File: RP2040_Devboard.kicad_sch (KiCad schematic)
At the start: 39 parts, among them J1 USB_B_Mini, J2 Conn_01x03_Socket, J3 Conn_01x22, J5 Conn_01x22, SW1 SW_Push, SW2 SW_Push, U1 RP2040, U2 AP2112K-1.2, U3 USBLC6-2SC6, U4 W25Q128JVS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

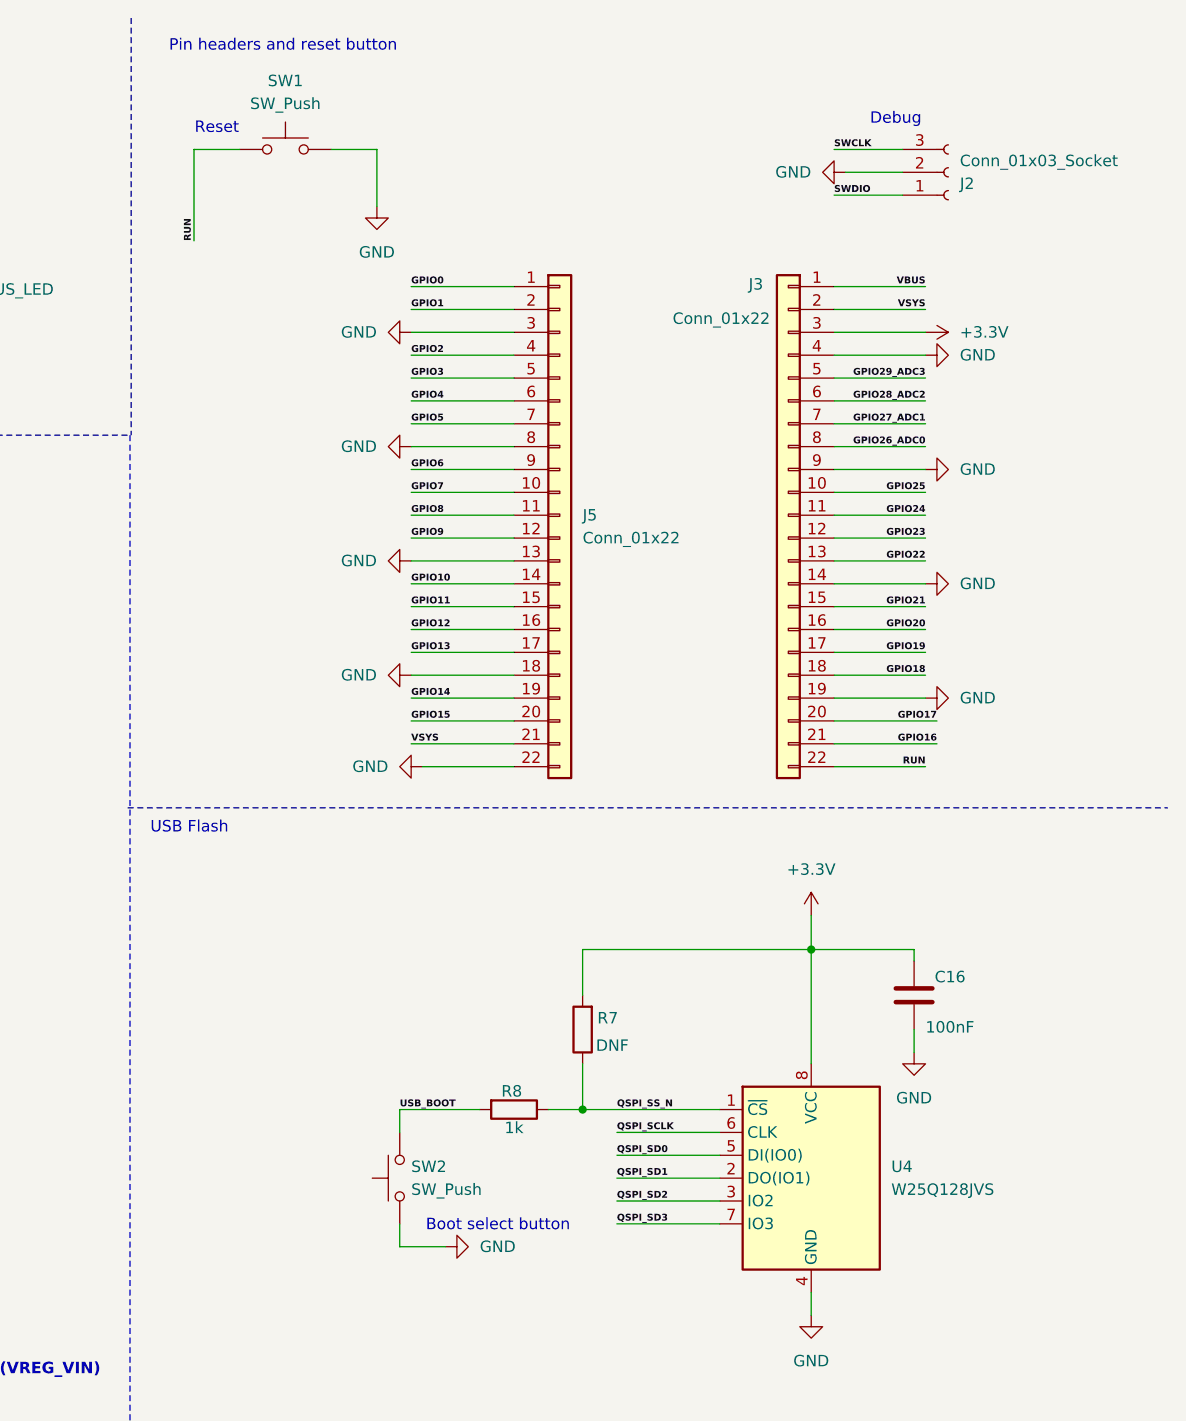
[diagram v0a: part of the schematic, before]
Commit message: Added RC for each button, deleted extra pins
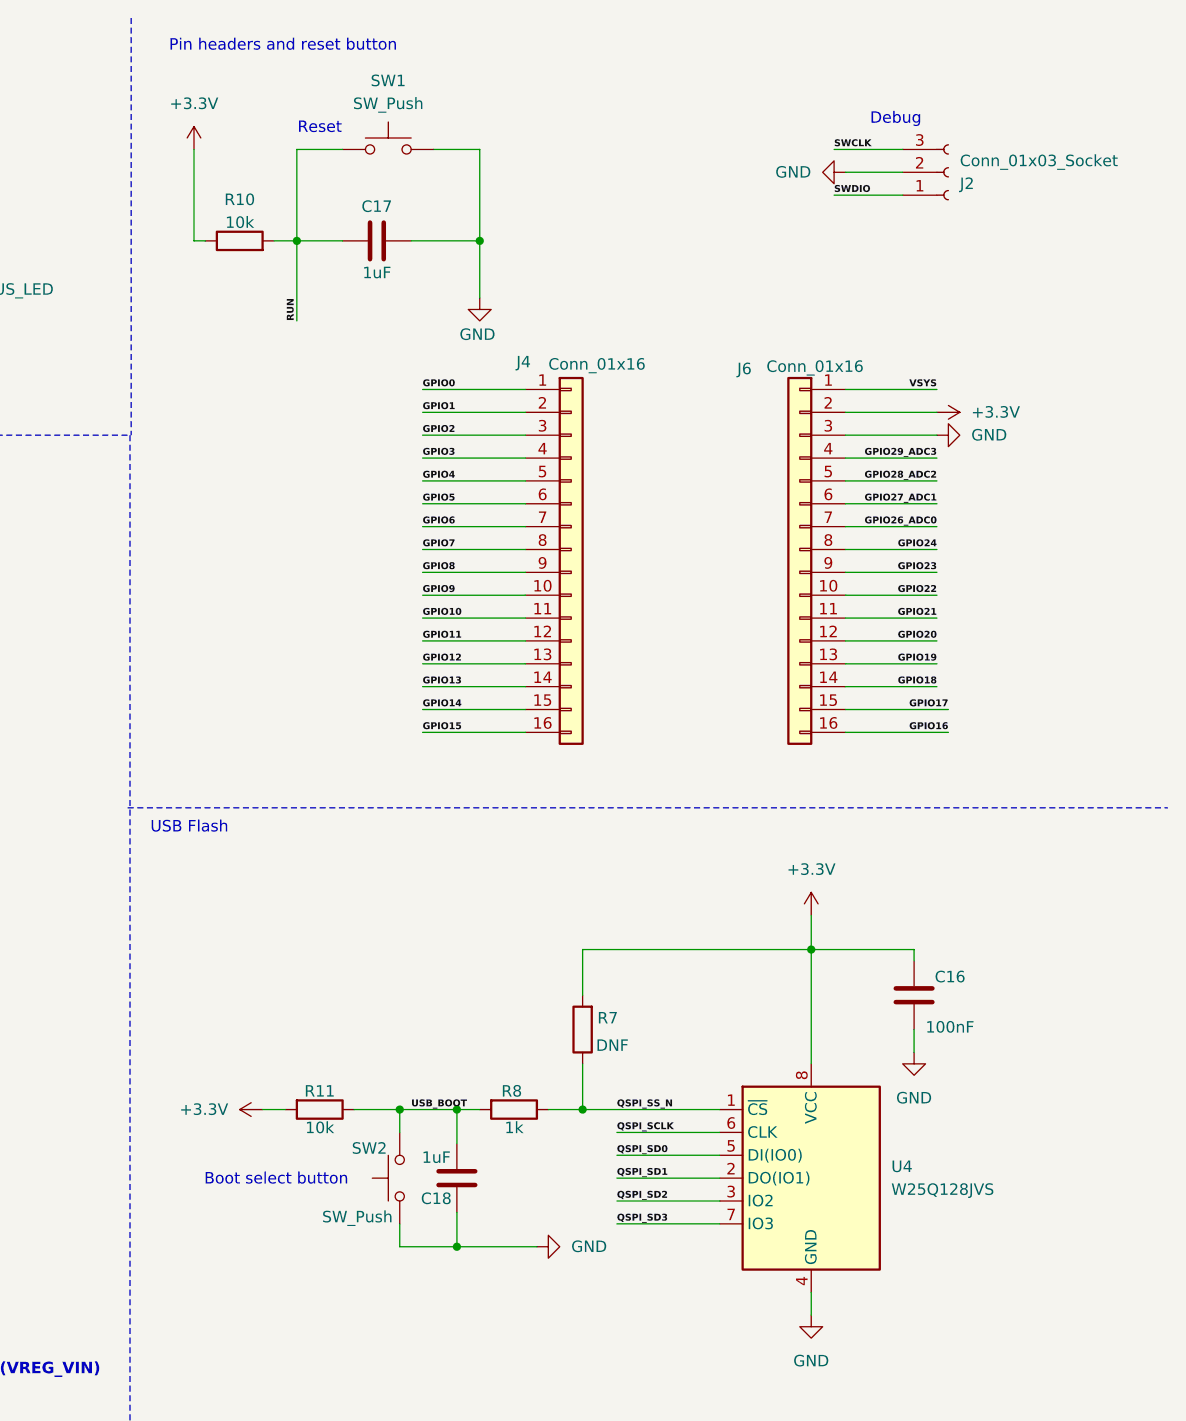
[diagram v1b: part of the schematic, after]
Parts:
- removed J3, J5: Conn_01x22, Connector_PinSocket_2.54mm:PinSocket_1x22_P2.54mm_Vertical, symbol Connector_Generic:Conn_01x22
- added C17, C18: 1uF, Capacitor_SMD:C_0805_2012Metric, symbol Device:C
- added J4, J6: Conn_01x16, Connector_PinSocket_2.54mm:PinSocket_1x16_P2.54mm_Vertical, symbol Connector_Generic:Conn_01x16
- added R10, R11: 10k, Resistor_SMD:R_0805_2012Metric, symbol Device:R
- U2: JLCPCB (none) -> https://jlcpcb.com/parts/componentSearch?searchTxt=AP2112K-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
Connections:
- net +3.3V: now also J6.2 (Pin_2), R10.1, R11.2
- net GND: now also C17.2, C18.2, J6.3 (Pin_3)
- net GPIO0: now also J4.1 (Pin_1)
- net GPIO1: now also J4.2 (Pin_2)
- net GPIO10: now also J4.11 (Pin_11)
- net GPIO11: now also J4.12 (Pin_12)
- net GPIO12: now also J4.13 (Pin_13)
- net GPIO13: now also J4.14 (Pin_14)
- net GPIO14: now also J4.15 (Pin_15)
- net GPIO15: now also J4.16 (Pin_16)
- net GPIO16: now also J6.16 (Pin_16)
- net GPIO17: now also J6.15 (Pin_15)
- net GPIO18: now also J6.14 (Pin_14)
- net GPIO19: now also J6.13 (Pin_13)
- net GPIO2: now also J4.3 (Pin_3)
- net GPIO20: now also J6.12 (Pin_12)
- net GPIO21: now also J6.11 (Pin_11)
- net GPIO22: now also J6.10 (Pin_10)
- net GPIO23: now also J6.9 (Pin_9)
- net GPIO24: now also J6.8 (Pin_8)
- net GPIO26_ADC0: now also J6.7 (Pin_7)
- net GPIO27_ADC1: now also J6.6 (Pin_6)
- net GPIO28_ADC2: now also J6.5 (Pin_5)
- net GPIO29_ADC3: now also J6.4 (Pin_4)
- net GPIO3: now also J4.4 (Pin_4)
- net GPIO4: now also J4.5 (Pin_5)
- net GPIO5: now also J4.6 (Pin_6)
- net GPIO6: now also J4.7 (Pin_7)
- net GPIO7: now also J4.8 (Pin_8)
- net GPIO8: now also J4.9 (Pin_9)
- net GPIO9: now also J4.10 (Pin_10)
- net RUN: now also C17.1, R10.2
- net USB_BOOT: now also C18.1, R11.1
- net VSYS: now also J6.1 (Pin_1)
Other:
- moved on the sheet: SW1

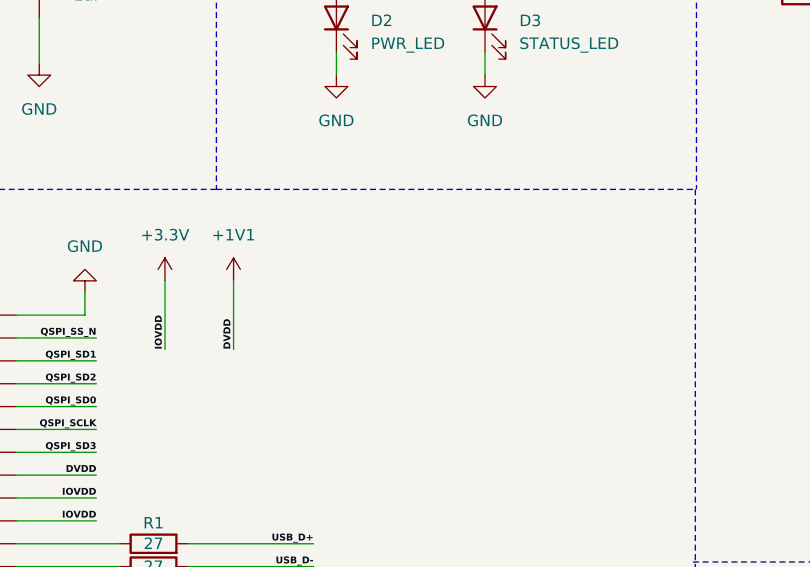
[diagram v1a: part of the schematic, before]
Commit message: Added mointing holes and stetching vias
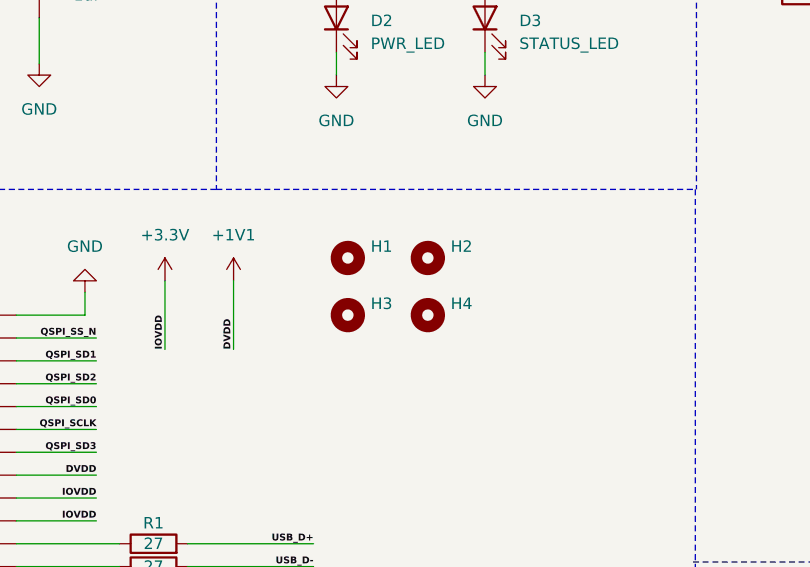
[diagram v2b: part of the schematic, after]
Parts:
- added H1, H2, H3, H4: MountingHole, MountingHole:MountingHole_3mm, symbol Mechanical:MountingHole
- J2: footprint Connector_PinHeader_2.54mm:PinHeader_1x03_P2.54mm_Horizontal -> Connector_PinHeader_2.54mm:PinHeader_1x03_P2.54mm_Vertical
